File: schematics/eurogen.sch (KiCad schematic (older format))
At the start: 23 parts, among them J1 PJ301M-12, J3 PJ301M-12, J4 EURO_PWR_2x5, SW1 Rotary_Encoder, U1 ESP32-DEVKITC-32D, U2 CODECODER-WM8731SEDS_V(SSOP28), U3 MCP3208

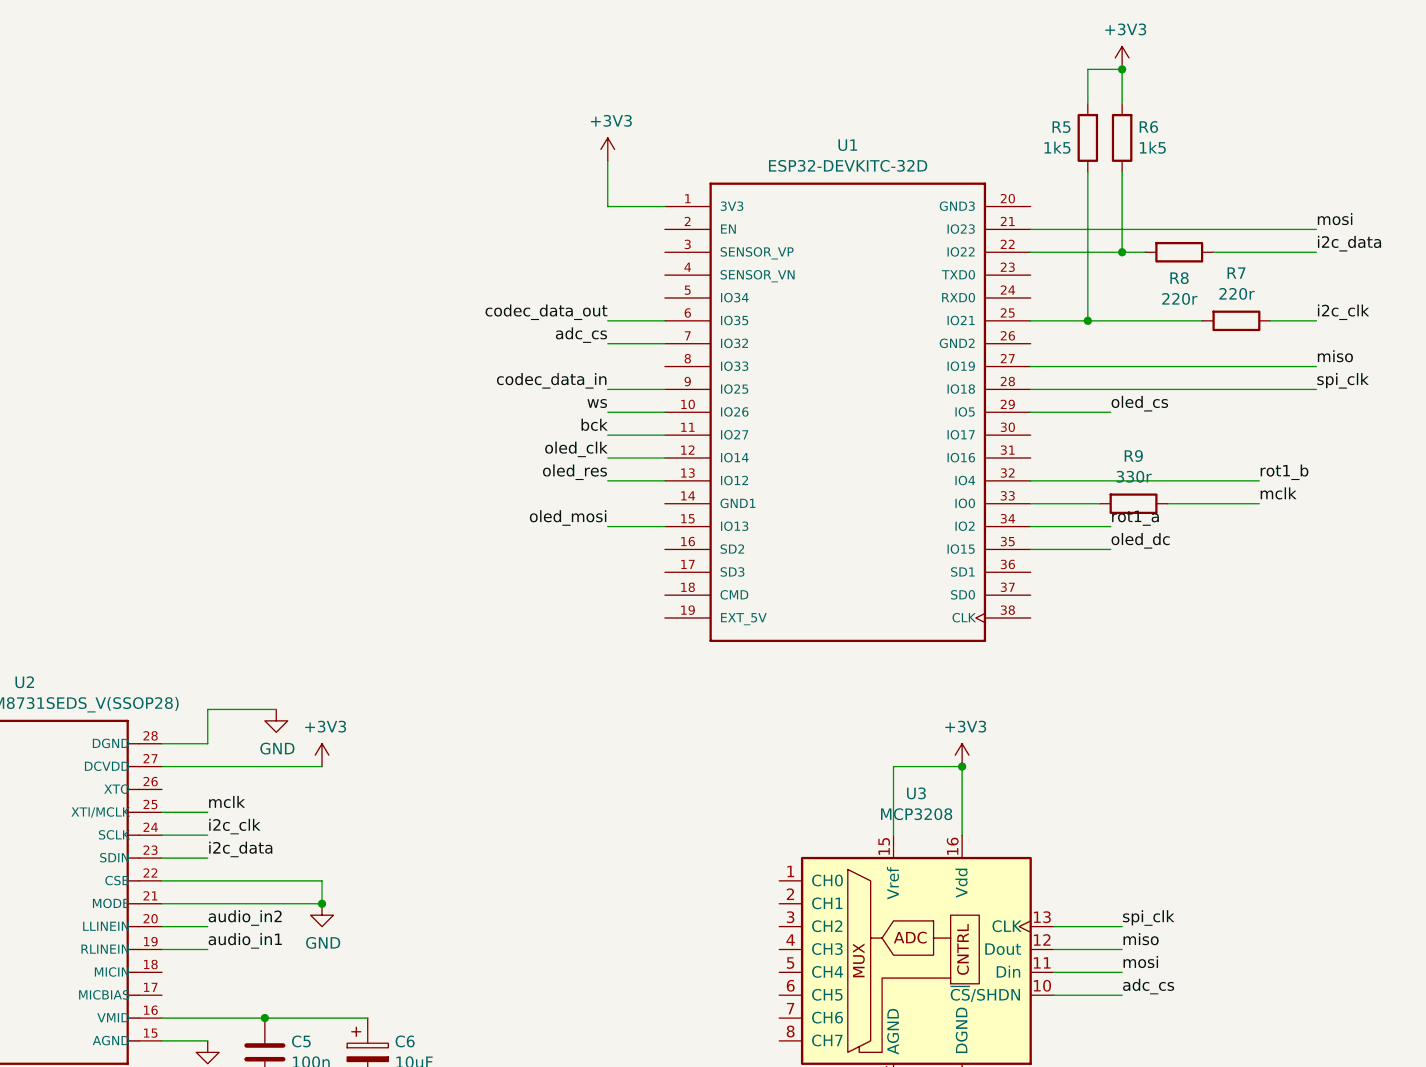
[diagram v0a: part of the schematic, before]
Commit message: WM8731 i2c fixed
changed resistor values
confirmed schematic
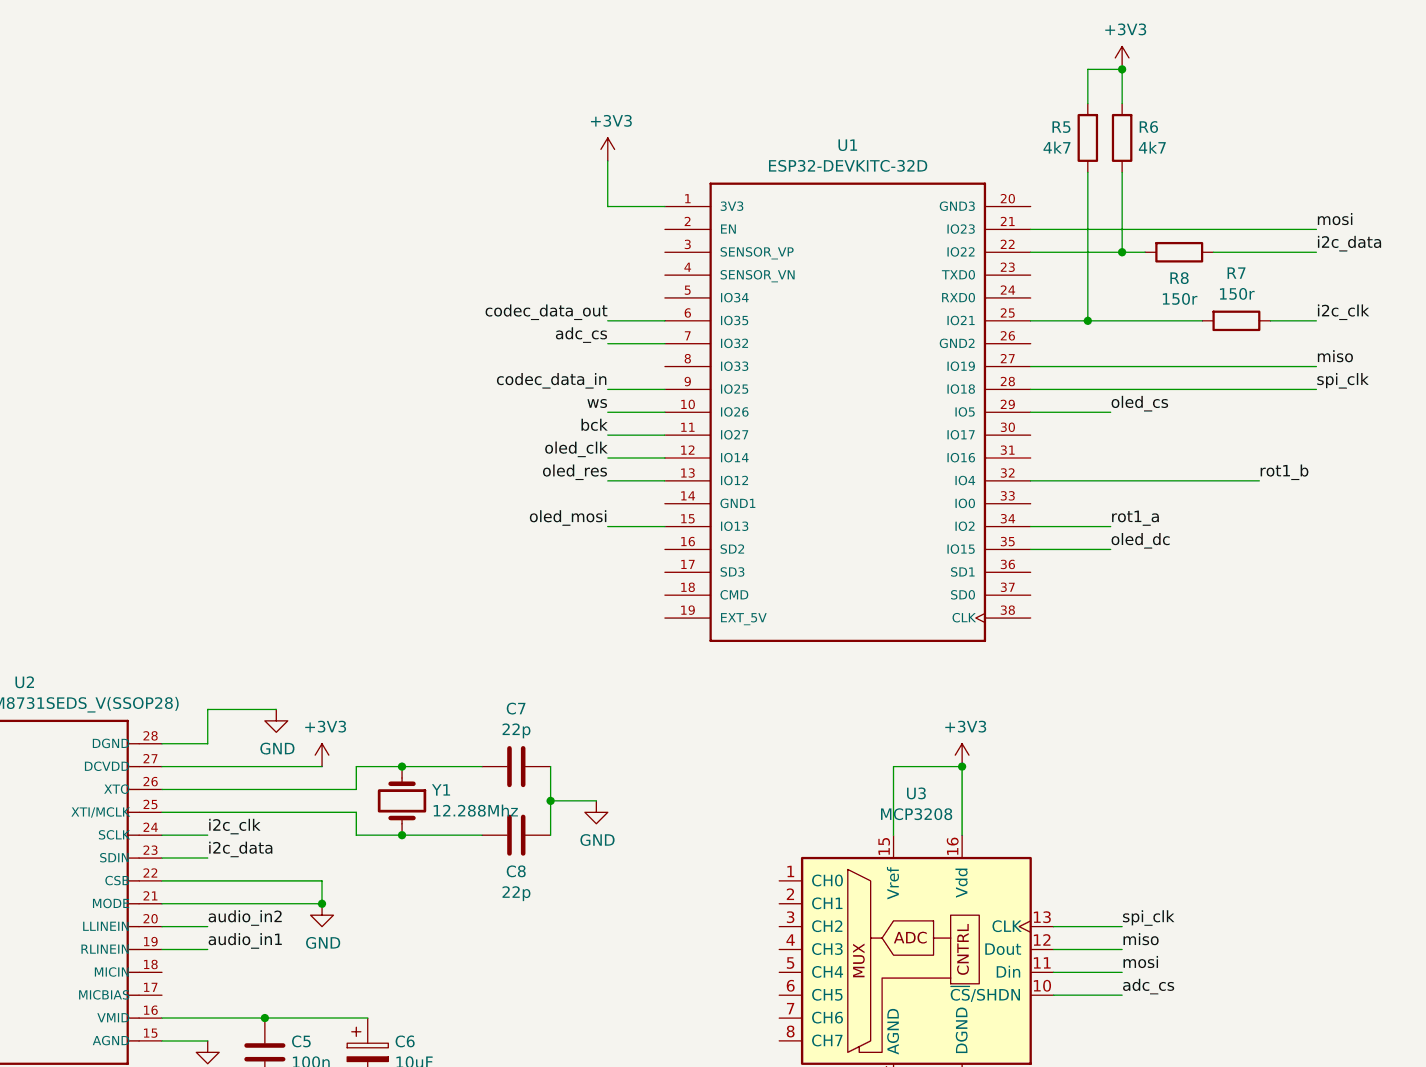
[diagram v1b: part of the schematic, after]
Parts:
- removed R9: 330r, symbol Device:R
- added C7, C8: 22p, symbol Device:C
- added Y1: 12.288Mhz, symbol Device:Crystal
- R5, R6: value 1k5 -> 4k7
- R7, R8: value 220r -> 150r
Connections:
- net GND: now also C7.1, C8.1
- net at U2.26 (XTO): now also C7.2, Y1.1
- net mclk: no longer names the net of U2.25 (XTI/MCLK)
- net mclk: now also C8.2, Y1.2
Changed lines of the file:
@@
 P 10450 1850
 F 0 "R7" V 10243 1850 50  0000 C CNN
-F 1 "220r" V 10334 1850 50  0000 C CNN
+F 1 "150r" V 10334 1850 50  0000 C CNN
 F 2 "" V 10380 1850 50  0001 C CNN
 F 3 "~" H 10450 1850 50  0001 C CNN
@@
 P 9950 1050
 F 0 "R6" H 9880 1004 50  0000 R CNN
-F 1 "1k5" H 9880 1095 50  0000 R CNN
+F 1 "4k7" H 9880 1095 50  0000 R CNN
 F 2 "" V 9880 1050 50  0001 C CNN
 F 3 "~" H 9950 1050 50  0001 C CNN
@@
 P 9800 1050
 F 0 "R5" H 9870 1004 50  0000 L CNN
-F 1 "1k5" H 9870 1095 50  0000 L CNN
+F 1 "4k7" H 9870 1095 50  0000 L CNN
 F 2 "" V 9730 1050 50  0001 C CNN
 F 3 "~" H 9800 1050 50  0001 C CNN
@@
 	9800 750  9950 750
 Connection ~ 9950 750
-Text Label 5950 4000 0    50   ~ 0
-mclk
-Wire Wire Line
-	5950 4000 5750 4000
-Text Label 10550 2650 0    50   ~ 0
-mclk
-Wire Wire Line
-	9850 2650 9550 2650
-$Comp
-L Device:R R9
-U 1 1 5E5CF849
-P 10000 2650
-F 0 "R9" V 9793 2650 50  0000 C CNN
-F 1 "330r" V 9884 2650 50  0000 C CNN
-F 2 "" V 9930 2650 50  0001 C CNN
-F 3 "~" H 10000 2650 50  0001 C CNN
-	1    10000 2650
-	0    1    1    0
-$EndComp
-Wire Wire Line
-	10150 2650 10550 2650
 $Comp
 L power:+3V3 #PWR017
@@
 P 10200 1550
 F 0 "R8" V 10315 1550 50  0000 C CNN
-F 1 "220r" V 10406 1550 50  0000 C CNN
+F 1 "150r" V 10406 1550 50  0000 C CNN
 F 2 "" V 10130 1550 50  0001 C CNN
 F 3 "~" H 10200 1550 50  0001 C CNN
@@
 Wire Wire Line
 	7700 1950 7950 1950
+$Comp
+L Device:Crystal Y1
+U 1 1 5E67AAEF
+P 6800 3950
+F 0 "Y1" V 6754 4081 50  0000 L CNN
+F 1 "12.288Mhz" V 6845 4081 50  0000 L CNN
+F 2 "" H 6800 3950 50  0001 C CNN
+F 3 "~" H 6800 3950 50  0001 C CNN
+	1    6800 3950
+	0    1    1    0
+$EndComp
+Wire Wire Line
+	5750 3900 6600 3900
+Wire Wire Line
+	6600 3900 6600 3800
+Wire Wire Line
+	6600 3800 6800 3800
+Wire Wire Line
+	5750 4000 6600 4000
+Wire Wire Line
+	6600 4000 6600 4100
+Wire Wire Line
+	6600 4100 6800 4100
+$Comp
+L Device:C C7
+U 1 1 5E683821
+P 7300 3800
+F 0 "C7" V 7048 3800 50  0000 C CNN
+F 1 "22p" V 7139 3800 50  0000 C CNN
+F 2 "" H 7338 3650 50  0001 C CNN
+F 3 "~" H 7300 3800 50  0001 C CNN
+	1    7300 3800
+	0    1    1    0
+$EndComp
+$Comp
+L Device:C C8
+U 1 1 5E684988
+P 7300 4100
+F 0 "C8" V 7460 4100 50  0000 C CNN
+F 1 "22p" V 7551 4100 50  0000 C CNN
+F 2 "" H 7338 3950 50  0001 C CNN
+F 3 "~" H 7300 4100 50  0001 C CNN
+	1    7300 4100
+	0    1    1    0
+$EndComp
+$Comp
+L power:GND #PWR023
+U 1 1 5E684DC7
+P 7650 3950
+F 0 "#PWR023" H 7650 3700 50  0001 C CNN
+F 1 "GND" H 7655 3777 50  0000 C CNN
+F 2 "" H 7650 3950 50  0001 C CNN
+F 3 "" H 7650 3950 50  0001 C CNN
+	1    7650 3950
+	1    0    0    -1
+$EndComp
+Wire Wire Line
+	6800 3800 7150 3800
+Connection ~ 6800 3800
+Wire Wire Line
+	6800 4100 7150 4100
+Connection ~ 6800 4100
+Wire Wire Line
+	7450 4100 7450 3950
+Wire Wire Line
+	7450 3950 7650 3950
+Connection ~ 7450 3950
+Wire Wire Line
+	7450 3950 7450 3800
 $EndSCHEMATC

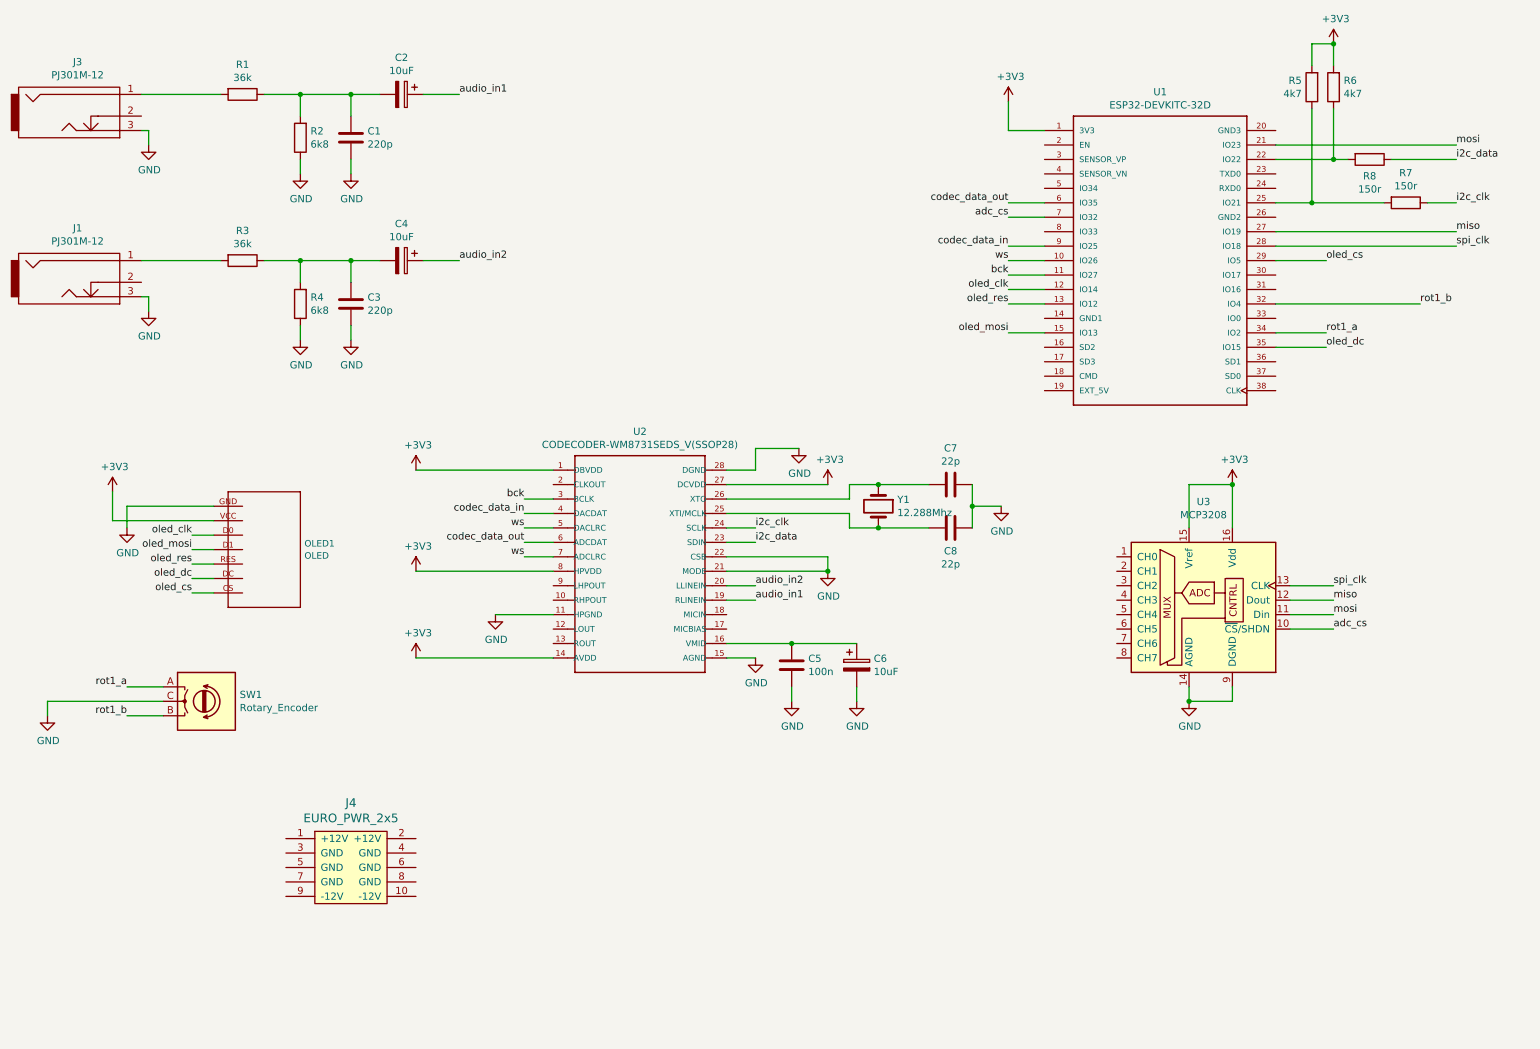
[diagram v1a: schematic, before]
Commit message: gpio updates, schematics update
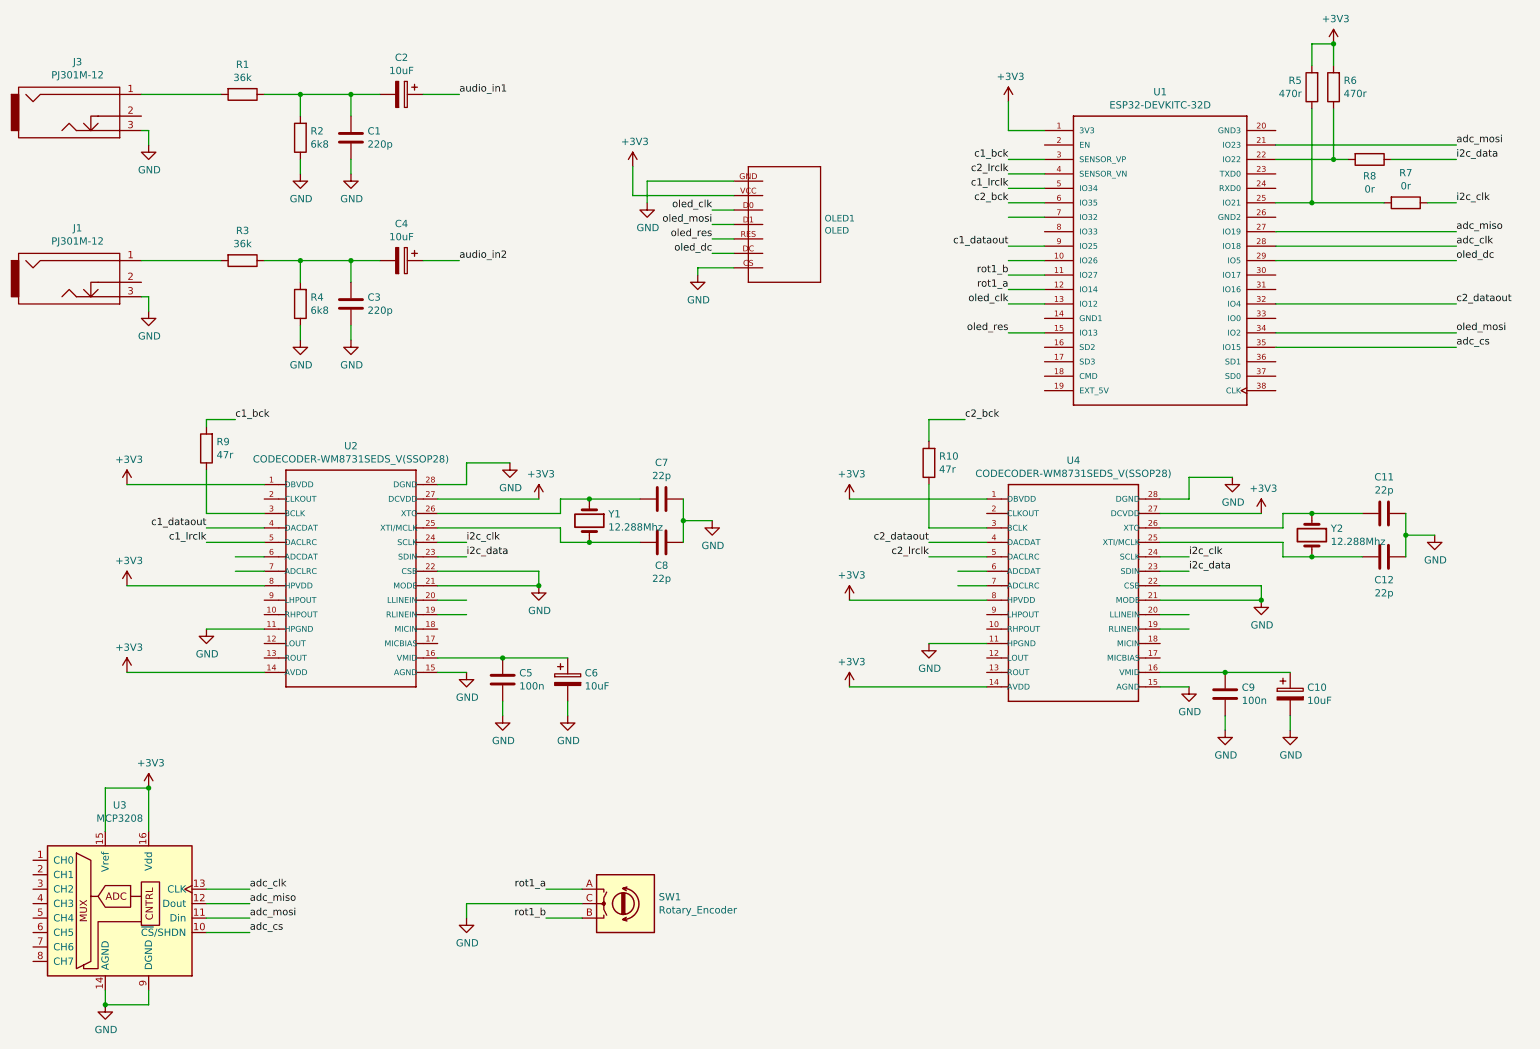
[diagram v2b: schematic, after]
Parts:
- removed J4: EURO_PWR_2x5, Connector_PinHeader_2.54mm:PinHeader_2x05_P2.54mm_Vertical, symbol eurocad:EURO_PWR_2x5
- added C10: 10uF, symbol Device:CP
- added C11, C12: 22p, symbol Device:C
- added C9: 100n, symbol Device:C
- added R10, R9: 47r, symbol Device:R
- added U4: CODECODER-WM8731SEDS_V(SSOP28), CODECODER-WM8731SEDS_V_SSOP28_:SSOP28-0.65-10.2X5.2MM, symbol CODECODER-WM8731SEDS_V_SSOP28_:CODECODER-WM8731SEDS_V(SSOP28)
- added Y2: 12.288Mhz, symbol Device:Crystal
- R5, R6: value 4k7 -> 470r
- R7, R8: value 150r -> 0r
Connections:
- net labels added: adc_clk, adc_miso, adc_mosi, c1_bck, c1_dataout, c1_lrclk, c2_bck, c2_dataout, c2_lrclk
- net labels removed: bck, codec_data_in, codec_data_out, miso, mosi, oled_cs, spi_clk, ws
- wire segments 109 -> 155
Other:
- moved on the sheet: C5, C6, C7, C8, OLED1, SW1, U2, U3, Y1

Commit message: schematic updates
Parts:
- added C13, C15, C16, C21, C23: 100n, symbol Device:C
- added C14: 100n, symbol Device:CP
- added C17, C18: 220uf, symbol Device:CP
- added C19, C20, C22: 47uf, symbol Device:CP
- added J10, J11, J12, J5, J6, J7, J8, J9: PJ301M-12, Eurocad:PJ301M-12, symbol eurocad:PJ301M-12
- added J2: EURO_PWR_2x5, symbol eurocad:EURO_PWR_2x5
- added J4: AudioJack3, symbol Connector:AudioJack3
- added R11, R17, R24, R25: 4k7, symbol Device:R
- added R12, R15, R16, R18, R22, R23, R26, R27: 27k, symbol Device:R
- added R13, R21, R28, R29: 1k, symbol Device:R
- added R14: 2k2, symbol Device:R
- added R19, R20: 47k, symbol Device:R
- added R30, R33, R36, R37: 200k, symbol Device:R
- added R31, R34, R38, R39: 100k, symbol Device:R
- added R32, R35, R40, R41: 33k, symbol Device:R
- added R42: 4r7, symbol Device:R
- added RV1, RV2, RV3, RV4: R_POT, symbol Device:R_POT
- added U10, U9: LM1117-3.3, symbol Regulator_Linear:LM1117-3.3
- added U5: TL074, symbol Amplifier_Operational:TL074
- added U6: LM4040LP-10, Package_TO_SOT_THT:TO-92_Inline, symbol Reference_Voltage:LM4040LP-10
- added U7, U8: MCP6004, symbol Amplifier_Operational:MCP6004
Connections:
- net labels added: +12V, +3.3VA, -12V, adc_ch0, adc_ch1, adc_ch2, adc_ch3, adc_ch4, adc_ch5, adc_ch6, adc_ch7, aref_-10v, c1_adc, c1_dac, c1_lhpout, c1_lout, c1_rhpout, c1_rout, c2_dac, c2_lout, c2_rout
- net labels removed: c1_dataout, c2_dataout
- wire segments 155 -> 397
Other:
- note added: "+5/-5V AC audio in -> 0dBu"
- note added: "CODEC out -> -5/+5V"
- note added: "CV in -> 0/3V3\n"
- note added: "stereo headphones out"
- moved on the sheet: C10, C11, C12, C5, C6, C7, C8, C9, R10, R9, SW1, U2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

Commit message: before cleanup
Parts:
- added C24, C25: 220p, symbol Device:C
- added C26, C27: 10uF, symbol Device:CP
- added J13, J14: PJ301M-12, Eurocad:PJ301M-12, symbol eurocad:PJ301M-12
- added R43, R44: 10k, symbol Device:R
- added R45, R46: 36k, symbol Device:R
- added R47, R48: 6k8, symbol Device:R
- added SW2, SW3: SW_Push, symbol Switch:SW_Push
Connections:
- net +3V3: now also SW2.2, SW3.2
- net GND: now also C24.2, C25.2, J13.3, J14.3, R43.1, R44.1, R47.1, R48.1
- net c2_lrclk: now also U4.7 (ADCLRC)
- net button1: now reaches U1.10 (IO26)
- net button1: now also R43.2, SW2.1
- net button2: now reaches U1.33 (IO0)
- net button2: now also R44.2, SW3.1
- net c2_adc: now reaches U1.8 (IO33)
- net c2_adc: now also U4.6 (ADCDAT)
- net audio_in4: now reaches U4.19 (RLINEIN)
- net audio_in4: now also C27.1
- net audio_in3: now reaches U4.20 (LLINEIN)
- net audio_in3: now also C26.1
- new net: J13.1, R45.2
- new net: C24.1, C26.2, R45.1, R47.2
- new net: J14.1, R46.2
- new net: C25.1, C27.2, R46.1, R48.2
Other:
- moved on the sheet: C10, C11, C12, C14, C5, C6, C7, C8, C9, J10, J11, J12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
